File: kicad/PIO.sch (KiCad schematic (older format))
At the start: 12 parts, among them J1 Conn_02x08_Odd_Even, J2 KMDGX-6S-BS, U15 Z84C20, U16 74AHC08, U18 74HC164, U19 74HC164, U2 74AHC14

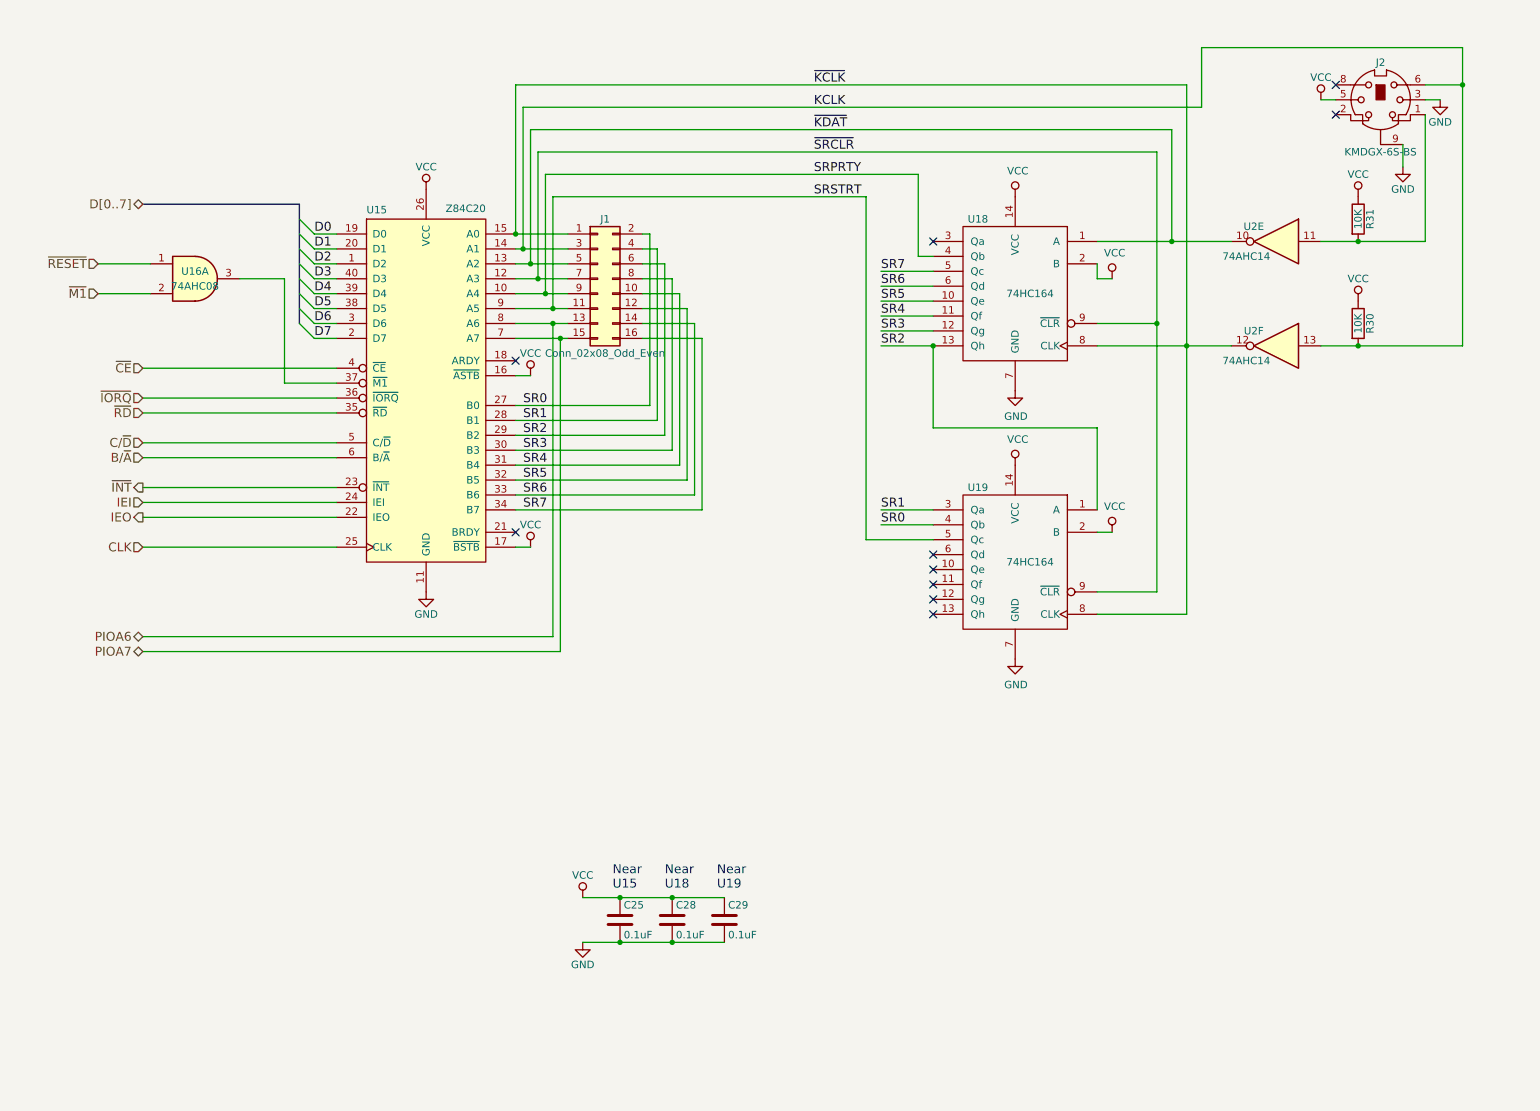
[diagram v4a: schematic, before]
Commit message: First complete version of ZED-80 schematic.
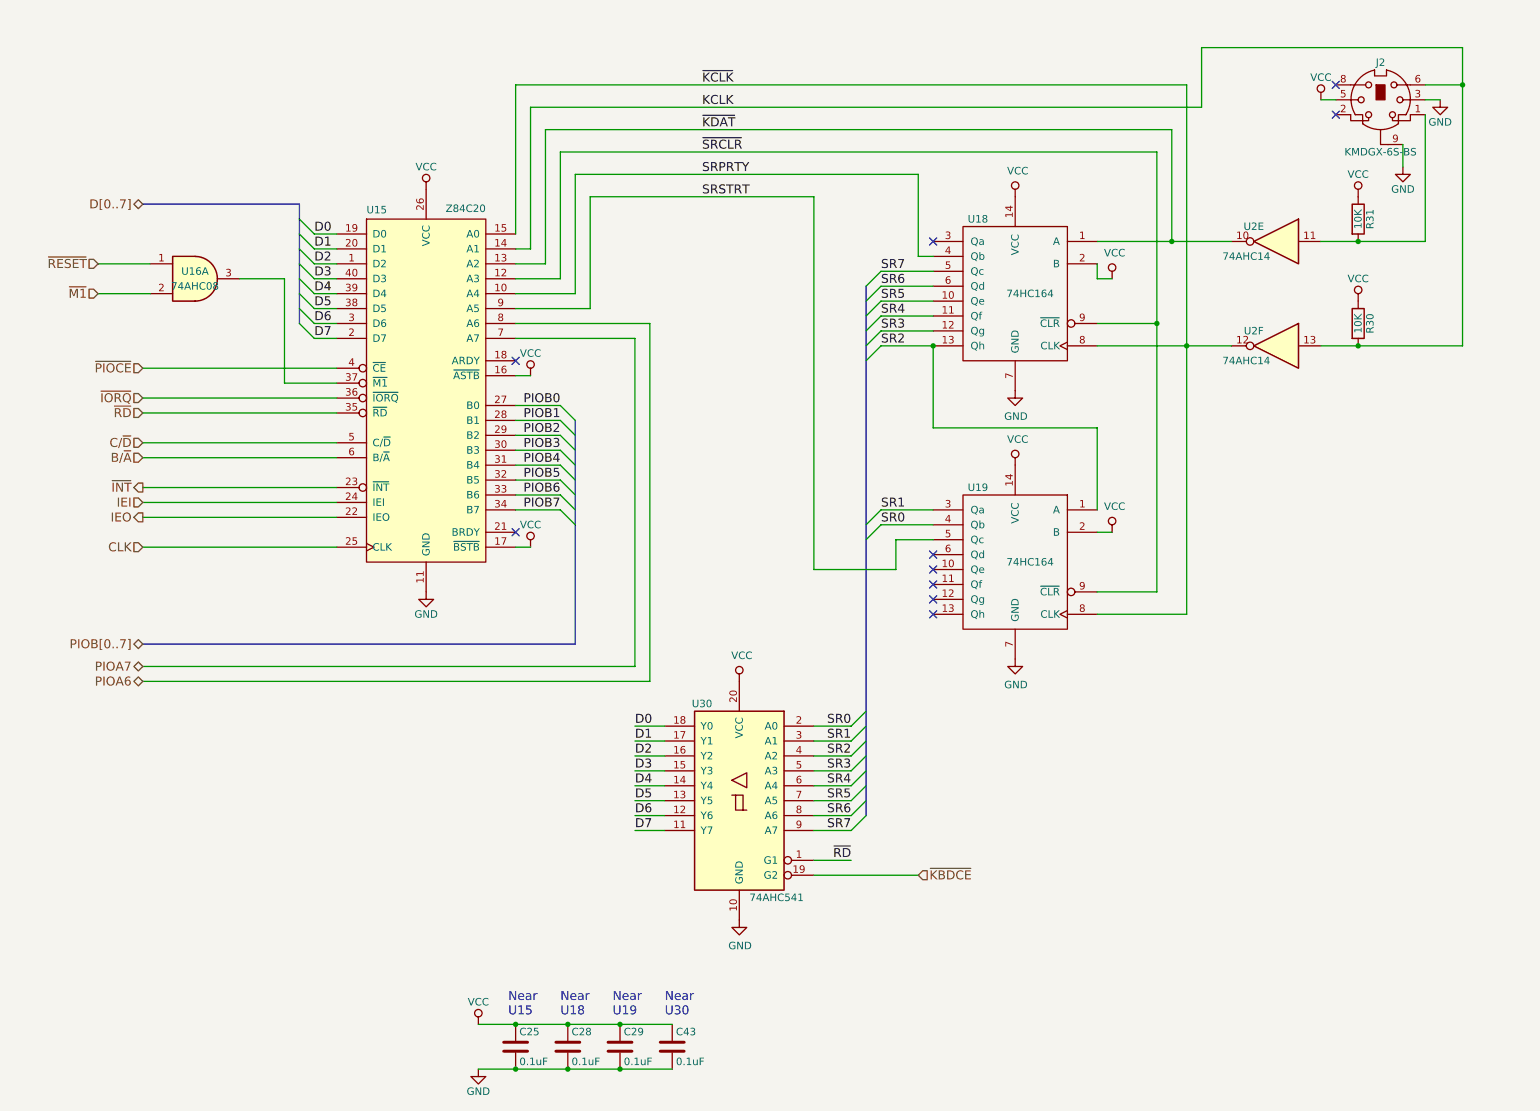
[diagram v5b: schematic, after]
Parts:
- removed J1: Conn_02x08_Odd_Even, Pin_Headers:Pin_Header_Straight_2x08_Pitch2.54mm, symbol Connector_Generic:Conn_02x08_Odd_Even
- added C43: 0.1uF, Capacitors_THT:C_Disc_D4.3mm_W1.9mm_P5.00mm, symbol Device:C
- added U30: 74AHC541, symbol 74xx:74LS541
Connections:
- net D0: now also U30.18 (Y0)
- net D1: now also U30.17 (Y1)
- net D2: now also U30.16 (Y2)
- net D3: now also U30.15 (Y3)
- net D4: now also U30.14 (Y4)
- net D5: now also U30.13 (Y5)
- net D6: now also U30.12 (Y6)
- net D7: now also U30.11 (Y7)
- net GND: now also C43.2, U30.10 (GND)
- net SR0: now also U30.2 (A0); no longer U15.27 (B0)
- net SR1: now also U30.3 (A1); no longer U15.28 (B1)
- net SR2: now also U30.4 (A2); no longer U15.29 (B2)
- net SR3: now also U30.5 (A3); no longer U15.30 (B3)
- net SR4: now also U30.6 (A4); no longer U15.31 (B4)
- net SR5: now also U30.7 (A5); no longer U15.32 (B5)
- net SR6: now also U30.8 (A6); no longer U15.33 (B6)
- net SR7: now also U30.9 (A7); no longer U15.34 (B7)
- net VCC: now also C43.1, U30.20 (VCC)
- net ~RD: now also U30.1 (G1)
- net ~CE renamed ~PIOCE
- new net PIOB0: U15.27 (B0)
- new net PIOB1: U15.28 (B1)
- new net PIOB2: U15.29 (B2)
- new net PIOB3: U15.30 (B3)
- new net PIOB4: U15.31 (B4)
- new net PIOB5: U15.32 (B5)
- new net PIOB6: U15.33 (B6)
- new net PIOB7: U15.34 (B7)
- new net ~KBDCE: U30.19 (G2)
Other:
- note added: "Near\nU30"
- moved on the sheet: C25, C28, C29

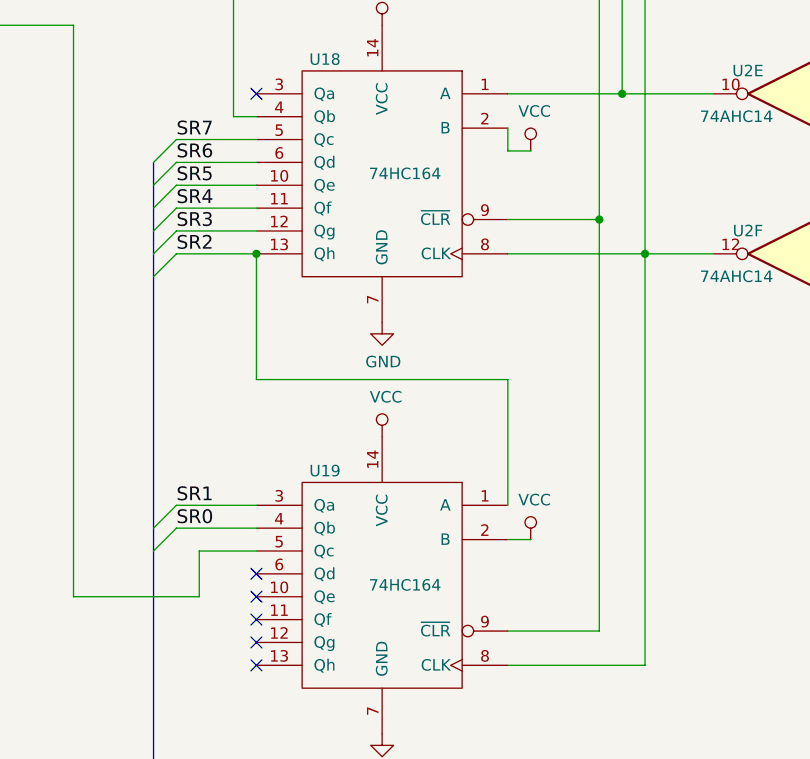
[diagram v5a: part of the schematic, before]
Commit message: Assign footprints.
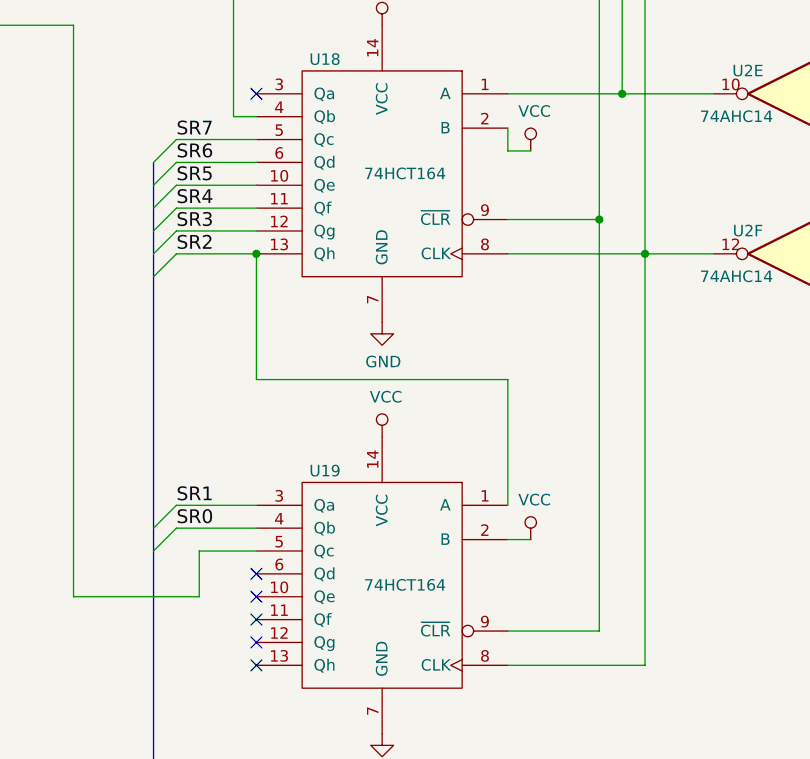
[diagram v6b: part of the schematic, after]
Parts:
- R30, R31: footprint Resistors_THT:R_Axial_DIN0204_L3.6mm_D1.6mm_P5.08mm_Horizontal -> Resistors_SMD:R_0805_HandSoldering
- U15: footprint Housings_DIP:DIP-40_W15.24mm_Socket_LongPads -> Housings_DIP:DIP-40_W15.24mm_Socket
- U16, U2: footprint Housings_DIP:DIP-14_W7.62mm_LongPads -> Housings_DIP:DIP-14_W7.62mm
- U18, U19: value 74HC164 -> 74HCT164; footprint Housings_DIP:DIP-14_W7.62mm_LongPads -> Housings_SSOP:TSSOP-14_4.4x5mm_Pitch0.65mm
- U30: footprint (none) -> Housings_SSOP:TSSOP-20_4.4x6.5mm_Pitch0.65mm
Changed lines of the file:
@@
 F 0 "U15" H 3000 4091 50  0000 L TNN
 F 1 "Z84C20" H 3800 4100 50  0000 R TNN
-F 2 "Housings_DIP:DIP-40_W15.24mm_Socket_LongPads" H 3800 4100 60  0001 C CNN
+F 2 "Housings_DIP:DIP-40_W15.24mm_Socket" H 3800 4100 60  0001 C CNN
 F 3 "" H 3800 4100 60  0001 C CNN
 	1    3400 3000
@@
 F 0 "U16" H 1850 2450 50  0000 C CNN
 F 1 "74AHC08" H 1850 2350 50  0000 C CNN
-F 2 "Housings_DIP:DIP-14_W7.62mm_LongPads" H 1850 2400 50  0001 C CNN
+F 2 "Housings_DIP:DIP-14_W7.62mm" H 1850 2400 50  0001 C CNN
 F 3 "" H 1850 2400 50  0001 C CNN
 	1    1850 2400
@@
 F 0 "R30" V 9730 2700 50  0000 C CNN
 F 1 "10K" V 9650 2700 50  0000 C CNN
-F 2 "Resistors_THT:R_Axial_DIN0204_L3.6mm_D1.6mm_P5.08mm_Horizontal" V 9580 2700 50  0001 C CNN
+F 2 "Resistors_SMD:R_0805_HandSoldering" V 9580 2700 50  0001 C CNN
 F 3 "" H 9650 2700 50  0001 C CNN
 	1    9650 2700
@@
 F 0 "R31" V 9730 2000 50  0000 C CNN
 F 1 "10K" V 9650 2000 50  0000 C CNN
-F 2 "Resistors_THT:R_Axial_DIN0204_L3.6mm_D1.6mm_P5.08mm_Horizontal" V 9580 2000 50  0001 C CNN
+F 2 "Resistors_SMD:R_0805_HandSoldering" V 9580 2000 50  0001 C CNN
 F 3 "" H 9650 2000 50  0001 C CNN
 	1    9650 2000
@@
 P 7350 2600
 F 0 "U18" H 7600 3200 50  0000 C CNN
-F 1 "74HC164" H 7250 2700 50  0000 C CNN
-F 2 "Housings_DIP:DIP-14_W7.62mm_LongPads" H 7200 2750 50  0001 C CNN
+F 1 "74HCT164" H 7250 2700 50  0000 C CNN
+F 2 "Housings_SSOP:TSSOP-14_4.4x5mm_Pitch0.65mm" H 7200 2750 50  0001 C CNN
 F 3 "" H 7200 2750 50  0001 C CNN
 	1    7350 2600
@@
 P 7350 4400
 F 0 "U19" H 7600 5000 50  0000 C CNN
-F 1 "74HC164" H 7250 4500 50  0000 C CNN
-F 2 "Housings_DIP:DIP-14_W7.62mm_LongPads" H 7200 4550 50  0001 C CNN
+F 1 "74HCT164" H 7250 4500 50  0000 C CNN
+F 2 "Housings_SSOP:TSSOP-14_4.4x5mm_Pitch0.65mm" H 7200 4550 50  0001 C CNN
 F 3 "" H 7200 4550 50  0001 C CNN
 	1    7350 4400
@@
 F 0 "U2" H 9250 2250 50  0000 C CNN
 F 1 "74AHC14" H 9300 2050 50  0000 C CNN
-F 2 "Housings_DIP:DIP-14_W7.62mm_LongPads" H 9100 2150 50  0001 C CNN
+F 2 "Housings_DIP:DIP-14_W7.62mm" H 9100 2150 50  0001 C CNN
 F 3 "" H 9100 2150 50  0001 C CNN
 	5    9100 2150
@@
 F 0 "U2" H 9250 2950 50  0000 C CNN
 F 1 "74AHC14" H 9300 2750 50  0000 C CNN
-F 2 "Housings_DIP:DIP-14_W7.62mm_LongPads" H 9100 2850 50  0001 C CNN
+F 2 "Housings_DIP:DIP-14_W7.62mm" H 9100 2850 50  0001 C CNN
 F 3 "" H 9100 2850 50  0001 C CNN
 	6    9100 2850
@@
 F 0 "U30" H 5750 6550 50  0000 C CNN
 F 1 "74AHC541" H 5250 5250 50  0000 C CNN
-F 2 "" H 5500 5900 50  0001 C CNN
+F 2 "Housings_SSOP:TSSOP-20_4.4x6.5mm_Pitch0.65mm" H 5500 5900 50  0001 C CNN
 F 3 "http://www.ti.com/lit/gpn/sn74LS541" H 5500 5900 50  0001 C CNN
 	1    5500 5900
